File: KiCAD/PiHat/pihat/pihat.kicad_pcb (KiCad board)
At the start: 2 copper layers, 64.8 x 55.9 mm, 45 parts, among them J1 Pan Servo Connector, J2 Tilt Servo Connector, J3 Fan, J4 Power Connector, P1 Conn_02x20_Odd_Even, P2 Pad, P3 Pad, P4 Pad, P5 Pad, P6 Pad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

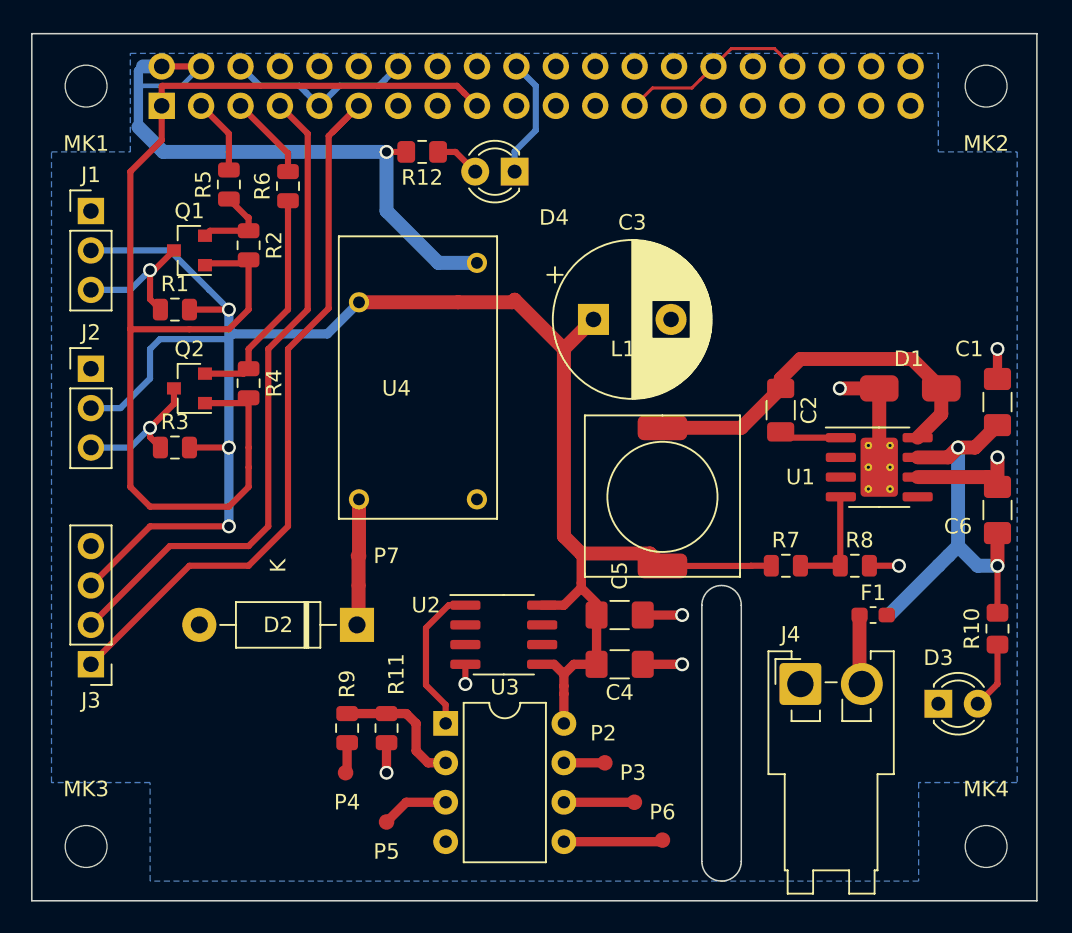
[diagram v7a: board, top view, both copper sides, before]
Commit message: Re-routing of components, fixed bugs from first spin
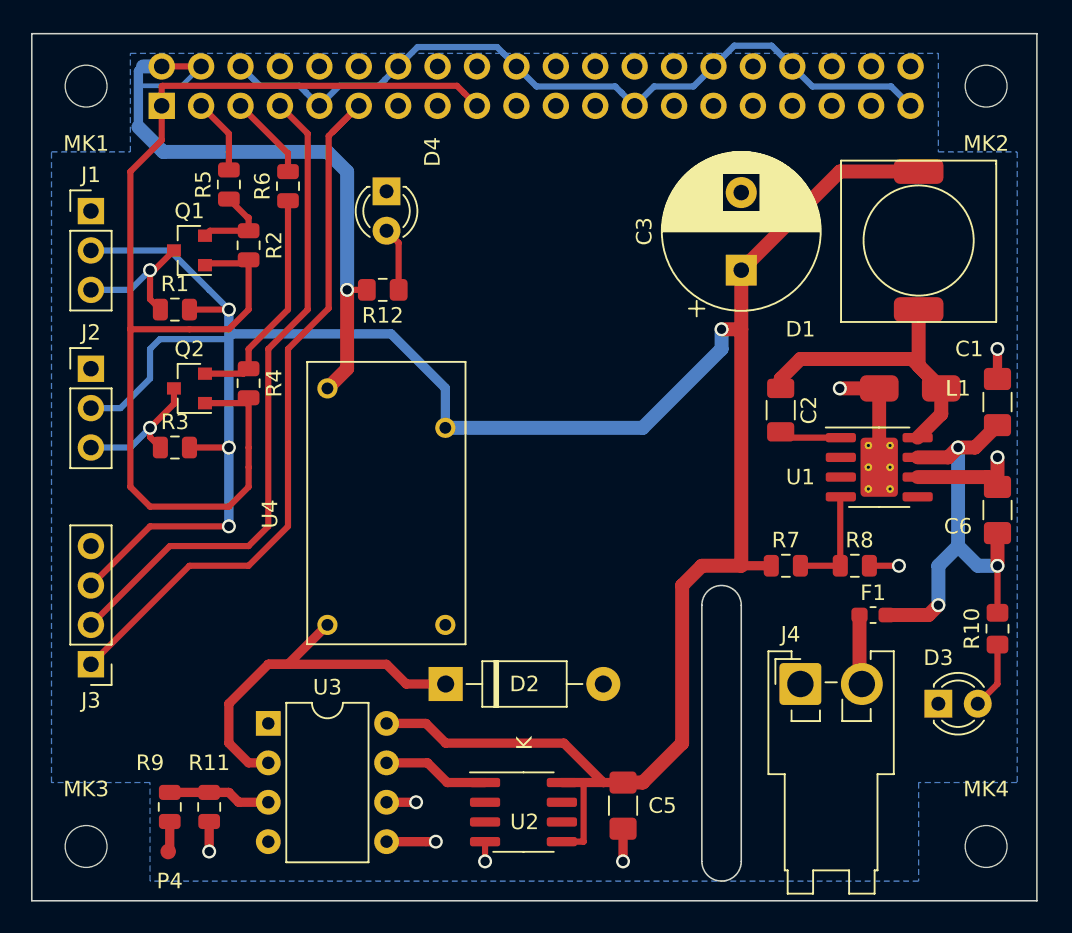
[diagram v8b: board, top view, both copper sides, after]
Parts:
- removed C4: 10nF, Resistor_SMD:R_1206_3216Metric_Pad1.42x1.75mm_HandSolder
- removed P2, P3, P5, P6, P7: Pad, trailTracer:Pad
- moved L1 18.2 mm to (257.1, 111.9), turned to 180 degrees
- moved P4 12.5 mm to (208.9, 146.8)
- moved R11 12.5 mm to (211.4, 144.0)
- moved R9 12.5 mm to (208.9, 144.0)
- moved C5 12.3 mm to (238.1, 143.9), turned to 270 degrees
- moved U2 11.5 mm to (231.7, 144.3)
- moved U3 11.4 mm to (215.2, 138.6)
- moved C3 10.0 mm to (245.7, 109.4), turned to 90 degrees
- moved R12 9.25 mm to (222.6, 110.6)
- moved D4 8.35 mm to (222.9, 104.3), turned to 270 degrees
- moved U4 8.34 mm to (217.7, 125.1)
- moved D2 6.87 mm to (226.7, 136.0), turned to 0 degrees
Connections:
- D2 pad 1: Net-(D2-Pad1) -> TINY_B4
- P1 pad 10: /GPIO15(RXD0) -> GPIO_15
- P1 pad 8: /GPIO14(TXD0) -> GPIO_14
- U2 pad 1: Net-(U2-Pad1) -> TINY_B2
- U3 pad 1: Net-(U2-Pad1) -> Net-(U3-Pad1)
- U3 pad 2: Net-(R11-Pad1) -> TINY_B4
- U3 pad 3: Net-(P5-Pad1) -> Net-(R11-Pad1)
- U3 pad 5: Net-(P6-Pad1) -> GPIO_15
- U3 pad 6: Net-(P3-Pad1) -> GPIO_14
- U3 pad 7: Net-(P2-Pad1) -> TINY_B2
- U4 pad 1: Net-(D2-Pad1) -> TINY_B4
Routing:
- net +5V: track 120.9 -> 171.5 mm, vias 3 -> 4
- net TINY_B4: track 0.00 -> 26.0 mm
- net GND: track 59.4 -> 74.8 mm, vias 8 -> 7
- net Net-(U2-Pad1): track 9.83 -> 0.00 mm
- net Net-(D2-Pad1): track 8.19 -> 0.00 mm
- net TINY_B2: track 0.00 -> 6.88 mm
- net Net-(P6-Pad1): track 6.39 -> 0.00 mm
- net Net-(P3-Pad1): track 4.55 -> 0.00 mm
- net Net-(P5-Pad1): track 4.34 -> 0.00 mm
- net GPIO_15: track 0.00 -> 3.32 mm, vias 0 -> 1
- net Net-(C2-Pad1): track 24.8 -> 21.8 mm
- net Net-(P2-Pad1): track 2.64 -> 0.00 mm
- net Net-(R11-Pad1): track 8.70 -> 6.61 mm
- net GPIO_14: track 0.00 -> 1.90 mm, vias 0 -> 1
- net +12V: track 26.8 -> 28.5 mm, vias 2 -> 3
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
